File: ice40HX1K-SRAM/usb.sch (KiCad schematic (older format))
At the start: 4 parts

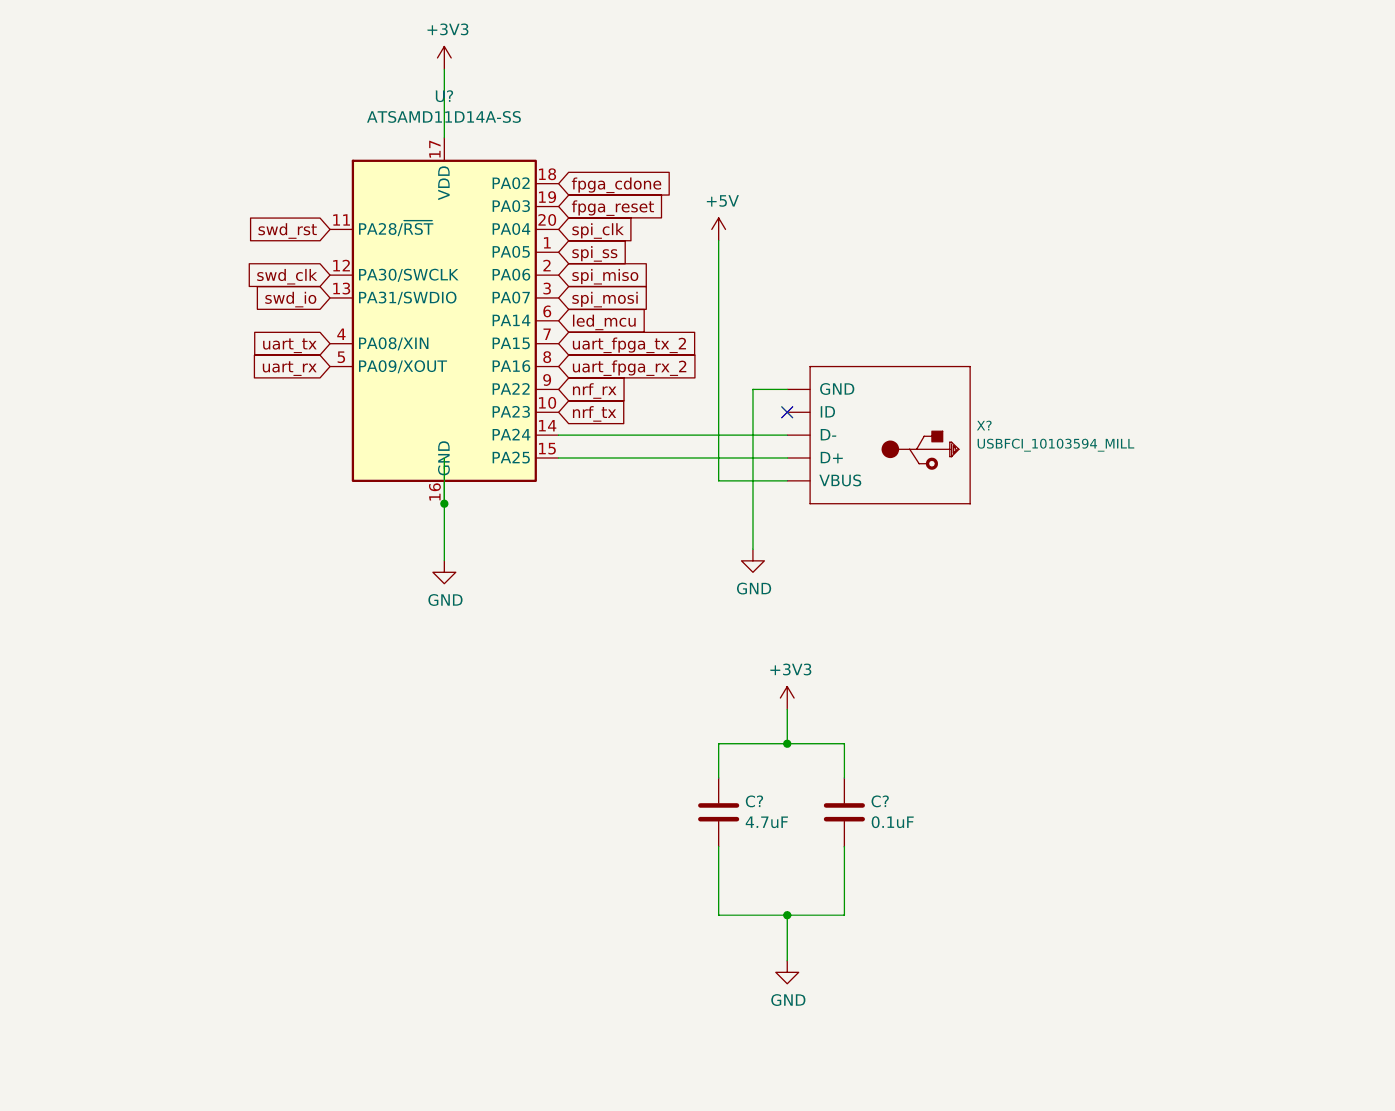
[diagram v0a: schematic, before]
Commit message: wiring FPGA nRF52 and ATSAMD11
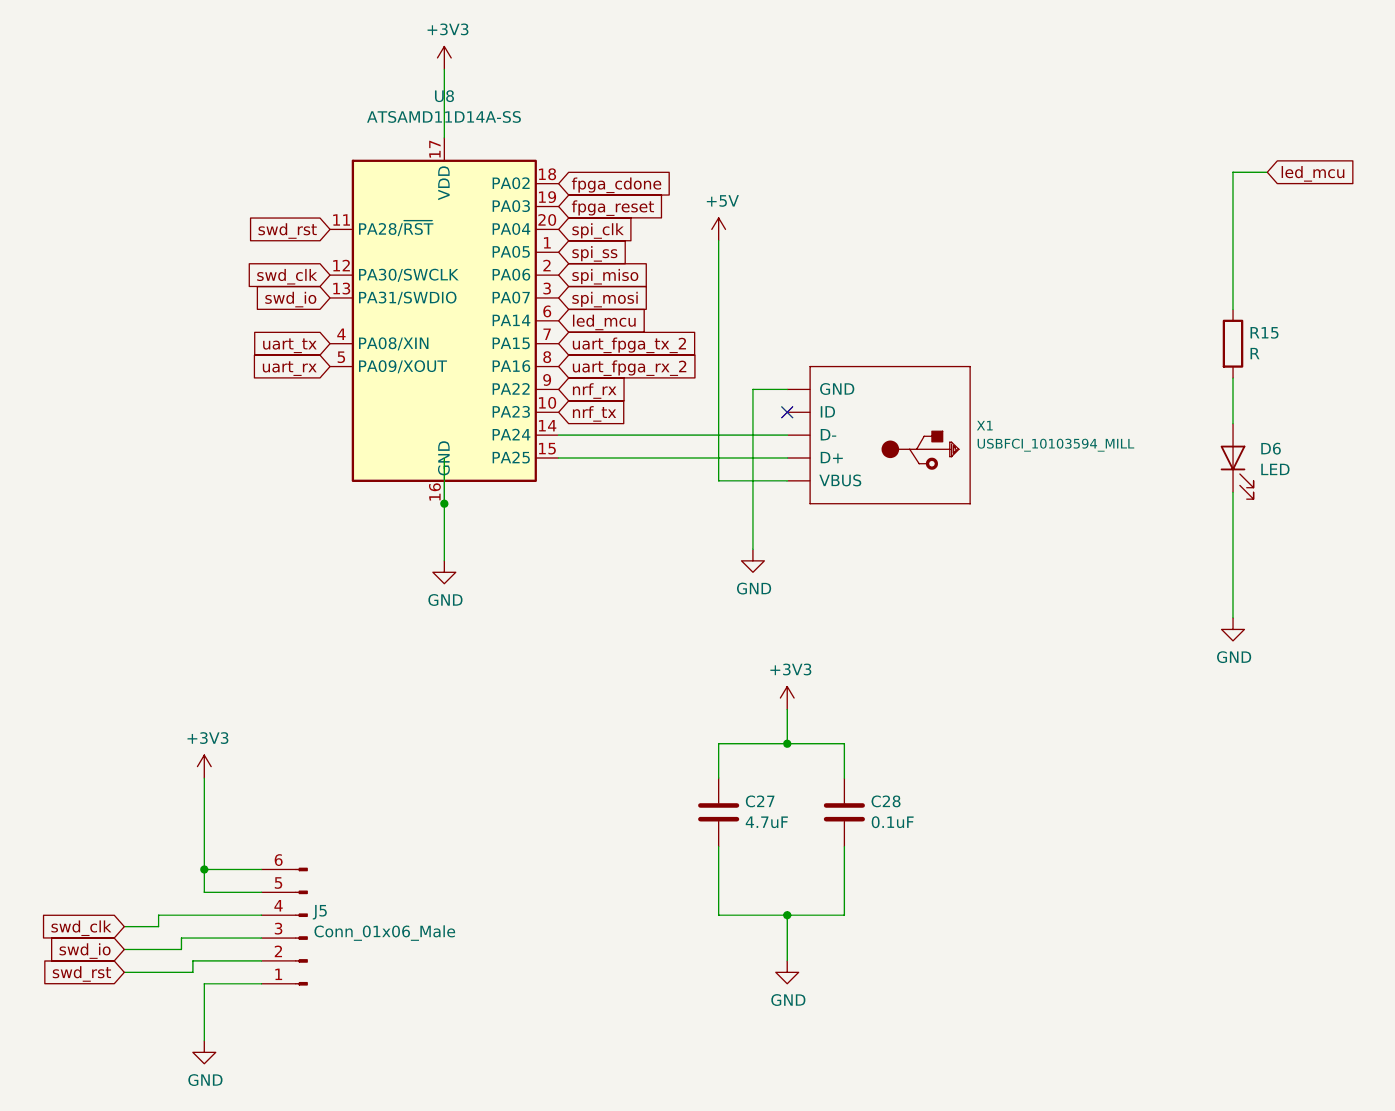
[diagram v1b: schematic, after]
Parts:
- added D6: LED, symbol Device:LED
- added J5: Conn_01x06_Male, symbol Connector:Conn_01x06_Male
- added R15: R, symbol Device:R
- gave numbers to parts that had none: 4
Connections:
- wire segments 19 -> 38
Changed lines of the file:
@@
 $EndDescr
 $Comp
-L cyUsb:USBFCI_10103594_MILL X?
+L cyUsb:USBFCI_10103594_MILL X1
 U 1 1 5E5FC52E
 P 4900 2700
-F 0 "X?" H 4472 2660 42  0000 R CNN
+F 0 "X1" H 4472 2660 42  0000 R CNN
 F 1 "USBFCI_10103594_MILL" H 4472 2739 42  0000 R CNN
 F 2 "" H 4900 2700 50  0001 C CNN
@@
 uart_rx
 $Comp
-L Device:C C?
+L Device:C C28
 U 1 1 5E6008C9
 P 4750 4350
-F 0 "C?" H 4865 4396 50  0000 L CNN
+F 0 "C28" H 4865 4396 50  0000 L CNN
 F 1 "0.1uF" H 4865 4305 50  0000 L CNN
 F 2 "" H 4788 4200 50  0001 C CNN
@@
 $EndComp
 $Comp
-L Device:C C?
+L Device:C C27
 U 1 1 5E6016EB
 P 4200 4350
-F 0 "C?" H 4315 4396 50  0000 L CNN
+F 0 "C27" H 4315 4396 50  0000 L CNN
 F 1 "4.7uF" H 4315 4305 50  0000 L CNN
 F 2 "" H 4238 4200 50  0001 C CNN
@@
 $EndComp
 $Comp
-L power:GND #PWR?
+L power:GND #PWR058
 U 1 1 5E601B3D
 P 4500 5000
-F 0 "#PWR?" H 4500 4750 50  0001 C CNN
+F 0 "#PWR058" H 4500 4750 50  0001 C CNN
 F 1 "GND" H 4505 4827 50  0000 C CNN
 F 2 "" H 4500 5000 50  0001 C CNN
@@
 $EndComp
 $Comp
-L power:+3V3 #PWR?
+L power:+3V3 #PWR057
 U 1 1 5E601EA6
 P 4500 3900
-F 0 "#PWR?" H 4500 3750 50  0001 C CNN
+F 0 "#PWR057" H 4500 3750 50  0001 C CNN
 F 1 "+3V3" H 4515 4073 50  0000 C CNN
 F 2 "" H 4500 3900 50  0001 C CNN
@@
 	4500 4800 4750 4800
 $Comp
-L power:GND #PWR?
+L power:GND #PWR056
 U 1 1 5E6043F3
 P 4350 3200
-F 0 "#PWR?" H 4350 2950 50  0001 C CNN
+F 0 "#PWR056" H 4350 2950 50  0001 C CNN
 F 1 "GND" H 4355 3027 50  0000 C CNN
 F 2 "" H 4350 3200 50  0001 C CNN
@@
 $EndComp
 $Comp
-L power:+3V3 #PWR?
+L power:+3V3 #PWR053
 U 1 1 5E604967
 P 3000 1100
-F 0 "#PWR?" H 3000 950 50  0001 C CNN
+F 0 "#PWR053" H 3000 950 50  0001 C CNN
 F 1 "+3V3" H 3015 1273 50  0000 C CNN
 F 2 "" H 3000 1100 50  0001 C CNN
@@
 $EndComp
 $Comp
-L power:+5V #PWR?
+L power:+5V #PWR055
 U 1 1 5E604F6F
 P 4200 1850
-F 0 "#PWR?" H 4200 1700 50  0001 C CNN
+F 0 "#PWR055" H 4200 1700 50  0001 C CNN
 F 1 "+5V" H 4215 2023 50  0000 C CNN
 F 2 "" H 4200 1850 50  0001 C CNN
@@
 led_mcu
 $Comp
-L GitRep_SAMD:ATSAMD11D14A-SS U?
+L GitRep_SAMD:ATSAMD11D14A-SS U8
 U 1 1 5E657B17
 P 3000 2200
-F 0 "U?" H 3000 3181 50  0000 C CNN
+F 0 "U8" H 3000 3181 50  0000 C CNN
 F 1 "ATSAMD11D14A-SS" H 3000 3090 50  0000 C CNN
 F 2 "Package_SO:SOIC-20W_7.5x12.8mm_P1.27mm" H 3000 1050 50  0001 C CNN
@@
 	4500 2800 3500 2800
 $Comp
-L power:GND #PWR?
+L power:GND #PWR054
 U 1 1 5E603984
 P 3000 3250
-F 0 "#PWR?" H 3000 3000 50  0001 C CNN
+F 0 "#PWR054" H 3000 3000 50  0001 C CNN
 F 1 "GND" H 3005 3077 50  0000 C CNN
 F 2 "" H 3000 3250 50  0001 C CNN
@@
 Text GLabel 3500 2600 2    50   Input ~ 0
 nrf_tx
+$Comp
+L power:GND #PWR?
+U 1 1 5E6748AE
+P 1950 5350
+AR Path="/5E5ECC92/5E6748AE" Ref="#PWR?"  Part="1"
+AR Path="/5E5EC834/5E6748AE" Ref="#PWR052"  Part="1"
+F 0 "#PWR052" H 1950 5100 50  0001 C CNN
+F 1 "GND" H 1955 5177 50  0000 C CNN
+F 2 "" H 1950 5350 50  0001 C CNN
+F 3 "" H 1950 5350 50  0001 C CNN
+	1    1950 5350
+	1    0    0    -1
+$EndComp
+Wire Wire Line
+	1950 5350 1950 5100
+Wire Wire Line
+	1950 5100 2200 5100
+Wire Wire Line
+	2200 4700 1950 4700
+Wire Wire Line
+	1950 4700 1950 4600
+Wire Wire Line
+	1950 4600 2200 4600
+Connection ~ 1950 4600
+Wire Wire Line
+	1950 4600 1950 4200
+Wire Wire Line
+	1600 4850 1750 4850
+Wire Wire Line
+	1750 4850 1750 4800
+Wire Wire Line
+	1750 4800 2200 4800
+Wire Wire Line
+	2200 4900 1850 4900
+Wire Wire Line
+	1850 4900 1850 4950
+Wire Wire Line
+	1850 4950 1600 4950
+$Comp
+L power:+3V3 #PWR051
+U 1 1 5E676D66
+P 1950 4200
+F 0 "#PWR051" H 1950 4050 50  0001 C CNN
+F 1 "+3V3" H 1965 4373 50  0000 C CNN
+F 2 "" H 1950 4200 50  0001 C CNN
+F 3 "" H 1950 4200 50  0001 C CNN
+	1    1950 4200
+	1    0    0    -1
+$EndComp
+$Comp
+L Connector:Conn_01x06_Male J5
+U 1 1 5E67B166
+P 2400 4900
+F 0 "J5" H 2372 4782 50  0000 R CNN
+F 1 "Conn_01x06_Male" H 2372 4873 50  0000 R CNN
+F 2 "" H 2400 4900 50  0001 C CNN
+F 3 "~" H 2400 4900 50  0001 C CNN
+	1    2400 4900
+	-1   0    0    1
+$EndComp
+Wire Wire Line
+	2200 5000 1900 5000
+Wire Wire Line
+	1900 5000 1900 5050
+Wire Wire Line
+	1900 5050 1600 5050
+Text GLabel 1600 4850 0    50   Input ~ 0
+swd_clk
+Text GLabel 1600 4950 0    50   Input ~ 0
+swd_io
+Text GLabel 1600 5050 0    50   Input ~ 0
+swd_rst
+Text GLabel 6600 1550 2    50   Input ~ 0
+led_mcu
+$Comp
+L Device:R R?
+U 1 1 5E6B28C3
+P 6450 2300
+AR Path="/5E5ECC92/5E6B28C3" Ref="R?"  Part="1"
+AR Path="/5E5EC834/5E6B28C3" Ref="R15"  Part="1"
+F 0 "R15" H 6520 2346 50  0000 L CNN
+F 1 "R" H 6520 2255 50  0000 L CNN
+F 2 "" V 6380 2300 50  0001 C CNN
+F 3 "~" H 6450 2300 50  0001 C CNN
+	1    6450 2300
+	1    0    0    -1
+$EndComp
+$Comp
+L Device:LED D?
+U 1 1 5E6B28C9
+P 6450 2800
+AR Path="/5E5ECC92/5E6B28C9" Ref="D?"  Part="1"
+AR Path="/5E5EC834/5E6B28C9" Ref="D6"  Part="1"
+F 0 "D6" V 6489 2683 50  0000 R CNN
+F 1 "LED" V 6398 2683 50  0000 R CNN
+F 2 "" H 6450 2800 50  0001 C CNN
+F 3 "~" H 6450 2800 50  0001 C CNN
+	1    6450 2800
+	0    -1   -1   0
+$EndComp
+$Comp
+L power:GND #PWR?
+U 1 1 5E6B28CF
+P 6450 3500
+AR Path="/5E5ECC92/5E6B28CF" Ref="#PWR?"  Part="1"
+AR Path="/5E5EC834/5E6B28CF" Ref="#PWR059"  Part="1"
+F 0 "#PWR059" H 6450 3250 50  0001 C CNN
+F 1 "GND" H 6455 3327 50  0000 C CNN
+F 2 "" H 6450 3500 50  0001 C CNN
+F 3 "" H 6450 3500 50  0001 C CNN
+	1    6450 3500
+	1    0    0    -1
+$EndComp
+Wire Wire Line
+	6450 3500 6450 2950
+Wire Wire Line
+	6450 2650 6450 2450
+Wire Wire Line
+	6450 2150 6450 1550
+Wire Wire Line
+	6450 1550 6600 1550
 $EndSCHEMATC

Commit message: wiring FPGA
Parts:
- C27, C28: footprint (none) -> Capacitor_SMD:C_0402_1005Metric
- J5: footprint (none) -> Connector_PinHeader_2.54mm:PinHeader_1x06_P2.54mm_Vertical
- R15: value R -> 10kOhm; footprint (none) -> Resistor_SMD:R_0402_1005Metric
- X1: footprint (none) -> kifootp:FCI_10103594_MILL
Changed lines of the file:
@@
 F 0 "X1" H 4472 2660 42  0000 R CNN
 F 1 "USBFCI_10103594_MILL" H 4472 2739 42  0000 R CNN
-F 2 "" H 4900 2700 50  0001 C CNN
+F 2 "kifootp:FCI_10103594_MILL" H 4900 2700 50  0001 C CNN
 F 3 "" H 4900 2700 50  0001 C CNN
 	1    4900 2700
@@
 F 0 "C28" H 4865 4396 50  0000 L CNN
 F 1 "0.1uF" H 4865 4305 50  0000 L CNN
-F 2 "" H 4788 4200 50  0001 C CNN
+F 2 "Capacitor_SMD:C_0402_1005Metric" H 4788 4200 50  0001 C CNN
 F 3 "~" H 4750 4350 50  0001 C CNN
 	1    4750 4350
@@
 F 0 "C27" H 4315 4396 50  0000 L CNN
 F 1 "4.7uF" H 4315 4305 50  0000 L CNN
-F 2 "" H 4238 4200 50  0001 C CNN
+F 2 "Capacitor_SMD:C_0402_1005Metric" H 4238 4200 50  0001 C CNN
 F 3 "~" H 4200 4350 50  0001 C CNN
 	1    4200 4350
@@
 F 0 "J5" H 2372 4782 50  0000 R CNN
 F 1 "Conn_01x06_Male" H 2372 4873 50  0000 R CNN
-F 2 "" H 2400 4900 50  0001 C CNN
+F 2 "Connector_PinHeader_2.54mm:PinHeader_1x06_P2.54mm_Vertical" H 2400 4900 50  0001 C CNN
 F 3 "~" H 2400 4900 50  0001 C CNN
 	1    2400 4900
@@
 AR Path="/5E5EC834/5E6B28C3" Ref="R15"  Part="1"
 F 0 "R15" H 6520 2346 50  0000 L CNN
-F 1 "R" H 6520 2255 50  0000 L CNN
-F 2 "" V 6380 2300 50  0001 C CNN
+F 1 "10kOhm" H 6520 2255 50  0000 L CNN
+F 2 "Resistor_SMD:R_0402_1005Metric" V 6380 2300 50  0001 C CNN
 F 3 "~" H 6450 2300 50  0001 C CNN
 	1    6450 2300

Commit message: starting layout
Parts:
- D6: footprint (none) -> LED_SMD:LED_1206_3216Metric
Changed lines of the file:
@@
 F 0 "D6" V 6489 2683 50  0000 R CNN
 F 1 "LED" V 6398 2683 50  0000 R CNN
-F 2 "" H 6450 2800 50  0001 C CNN
+F 2 "LED_SMD:LED_1206_3216Metric" H 6450 2800 50  0001 C CNN
 F 3 "~" H 6450 2800 50  0001 C CNN
 	1    6450 2800
